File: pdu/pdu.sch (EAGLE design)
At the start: 14 parts, among them IC1 FDN359BN, IC2 FDN359BN, IC3 FDN359BN

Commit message: add usb c (optional)
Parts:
- added C14: 100n, Capacitor:C_CHIP-0603(1608-METRIC)
- added C15: 1u, Capacitor:C_CHIP-0603(1608-METRIC)
- added D2: USBDiode, adafruit:DIODE_SOD-123FL
- added J6: USB4105-GF-A, USB4105-GF-A:USB4105-GF-A
- added R12, R14: 5k1, Resistor:R_CHIP-0603(1608-METRIC)
- added R13: 1M, Resistor:R_CHIP-0603(1608-METRIC)
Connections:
- net N$4 renamed RET
- new net CC1: J6.CC1, R14.1
- new net CC2: J6.CC2, R12.1
- new net SHLD: J6.SHELL_GND, R13.1
- new net VBUS: C14.2, C15.2, D2.A, J6.VBUS
- net GND: now also C14.1, C15.1, J6.GND, R12.2, R13.2, R14.2
- net VBAT: now also D2.C
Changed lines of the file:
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@@
 <part name="SUPPLY6" library="Power_Symbols" library_urn="urn:adsk.eagle:library:16502351" deviceset="GND-BAR" device="" value="GND"/>
 <part name="C3" library="Capacitor" library_urn="urn:adsk.eagle:library:16290819" deviceset="C" device="CHIP-0603(1608-METRIC)" package3d_urn="urn:adsk.eagle:package:16290898/5" technology="_" value="100p"/>
+<part name="SUPPLY24" library="Power_Symbols" library_urn="urn:adsk.eagle:library:16502351" deviceset="GND-BAR" device="" value="GND"/>
+<part name="R12" library="Resistor" library_urn="urn:adsk.eagle:library:16378527" deviceset="R" device="CHIP-0603(1608-METRIC)" package3d_urn="urn:adsk.eagle:package:16378565/5" technology="_" value="5k1"/>
+<part name="R13" library="Resistor" library_urn="urn:adsk.eagle:library:16378527" deviceset="R" device="CHIP-0603(1608-METRIC)" package3d_urn="urn:adsk.eagle:package:16378565/5" technology="_" value="1M"/>
+<part name="R14" library="Resistor" library_urn="urn:adsk.eagle:library:16378527" deviceset="R" device="CHIP-0603(1608-METRIC)" package3d_urn="urn:adsk.eagle:package:16378565/5" technology="_" value="5k1"/>
+<part name="D2" library="adafruit" library_urn="urn:adsk.eagle:library:420" deviceset="DIODE" device="_SOD-123FL" package3d_urn="urn:adsk.eagle:package:6240937/1" override_package3d_urn="urn:adsk.eagle:package:44099330/2" override_package_urn="urn:adsk.eagle:footprint:6240294/1" value="USBDiode"/>
+<part name="C14" library="Capacitor" library_urn="urn:adsk.eagle:library:16290819" deviceset="C" device="CHIP-0603(1608-METRIC)" package3d_urn="urn:adsk.eagle:package:16290898/5" technology="_" value="100n"/>
+<part name="C15" library="Capacitor" library_urn="urn:adsk.eagle:library:16290819" deviceset="C" device="CHIP-0603(1608-METRIC)" package3d_urn="urn:adsk.eagle:package:16290898/5" technology="_" value="1u"/>
+<part name="J6" library="USB4105-GF-A" deviceset="USB4105-GF-A" device=""/>
+<part name="SUPPLY48" library="Power_Symbols" library_urn="urn:adsk.eagle:library:16502351" deviceset="GND-BAR" device="" value="GND"/>
 </parts>
 <sheets>
@@
 <attribute name="NAME" x="-6.985" y="-71.755" size="1.778" layer="95" rot="R180"/>
 <attribute name="VALUE" x="-8.255" y="-67.31" size="1.778" layer="96" rot="R180"/>
+</instance>
+<instance part="SUPPLY24" gate="G$1" x="6.35" y="100.33" smashed="yes">
+<attribute name="VALUE" x="6.35" y="98.425" size="1.778" layer="96" align="center"/>
+</instance>
+<instance part="R12" gate="G$1" x="24.13" y="113.03" smashed="yes" rot="R270">
+<attribute name="NAME" x="26.67" y="113.03" size="1.778" layer="95" rot="R270" align="center"/>
+<attribute name="VALUE" x="21.59" y="113.03" size="1.778" layer="96" rot="R270" align="center"/>
+</instance>
+<instance part="R13" gate="G$1" x="13.97" y="113.03" smashed="yes" rot="R270">
+<attribute name="NAME" x="16.51" y="113.03" size="1.778" layer="95" rot="R270" align="center"/>
+<attribute name="VALUE" x="11.43" y="113.03" size="1.778" layer="96" rot="R270" align="center"/>
+</instance>
+<instance part="R14" gate="G$1" x="34.29" y="113.03" smashed="yes" rot="R270">
+<attribute name="NAME" x="36.83" y="113.03" size="1.778" layer="95" rot="R270" align="center"/>
+<attribute name="VALUE" x="31.75" y="113.03" size="1.778" layer="96" rot="R270" align="center"/>
+</instance>
+<instance part="D2" gate="G$1" x="19.05" y="138.43" smashed="yes">
+<attribute name="NAME" x="16.51" y="140.97" size="1.27" layer="95"/>
+<attribute name="VALUE" x="16.51" y="134.62" size="1.27" layer="96"/>
+</instance>
+<instance part="C14" gate="G$1" x="54.61" y="110.49" smashed="yes" rot="R180">
+<attribute name="NAME" x="60.325" y="109.855" size="1.778" layer="95" rot="R180"/>
+<attribute name="VALUE" x="60.325" y="116.84" size="1.778" layer="96" rot="R180"/>
+</instance>
+<instance part="C15" gate="G$1" x="44.45" y="110.49" smashed="yes" rot="R180">
+<attribute name="NAME" x="50.165" y="109.855" size="1.778" layer="95" rot="R180"/>
+<attribute name="VALUE" x="47.625" y="116.84" size="1.778" layer="96" rot="R180"/>
+</instance>
+<instance part="J6" gate="G$1" x="-49.53" y="124.46" smashed="yes">
+<attribute name="NAME" x="-64.77" y="138.43" size="1.778" layer="95"/>
+<attribute name="VALUE" x="-64.77" y="109.22" size="1.778" layer="96"/>
+</instance>
+<instance part="SUPPLY48" gate="G$1" x="-8.89" y="116.84" smashed="yes" rot="R90">
+<attribute name="VALUE" x="-6.985" y="116.84" size="1.778" layer="96" rot="R90" align="center"/>
 </instance>
 </instances>
@@
 <junction x="0" y="-77.47"/>
 </segment>
+<segment>
+<wire x1="1.27" y1="123.19" x2="6.35" y2="123.19" width="0.1524" layer="91"/>
+<pinref part="SUPPLY24" gate="G$1" pin="GND"/>
+<wire x1="6.35" y1="123.19" x2="6.35" y2="105.41" width="0.1524" layer="91"/>
+<pinref part="R13" gate="G$1" pin="2"/>
+<wire x1="6.35" y1="105.41" x2="6.35" y2="102.87" width="0.1524" layer="91"/>
+<wire x1="13.97" y1="107.95" x2="13.97" y2="105.41" width="0.1524" layer="91"/>
+<wire x1="13.97" y1="105.41" x2="6.35" y2="105.41" width="0.1524" layer="91"/>
+<junction x="6.35" y="105.41"/>
+<pinref part="R14" gate="G$1" pin="2"/>
+<wire x1="34.29" y1="107.95" x2="34.29" y2="105.41" width="0.1524" layer="91"/>
+<wire x1="34.29" y1="105.41" x2="24.13" y2="105.41" width="0.1524" layer="91"/>
+<junction x="13.97" y="105.41"/>
+<pinref part="R12" gate="G$1" pin="2"/>
+<wire x1="24.13" y1="105.41" x2="13.97" y2="105.41" width="0.1524" layer="91"/>
+<wire x1="24.13" y1="107.95" x2="24.13" y2="105.41" width="0.1524" layer="91"/>
+<junction x="24.13" y="105.41"/>
+<pinref part="C15" gate="G$1" pin="1"/>
+<wire x1="44.45" y1="107.95" x2="44.45" y2="105.41" width="0.1524" layer="91"/>
+<wire x1="44.45" y1="105.41" x2="34.29" y2="105.41" width="0.1524" layer="91"/>
+<junction x="34.29" y="105.41"/>
+<pinref part="C14" gate="G$1" pin="1"/>
+<wire x1="54.61" y1="107.95" x2="54.61" y2="105.41" width="0.1524" layer="91"/>
+<wire x1="54.61" y1="105.41" x2="44.45" y2="105.41" width="0.1524" layer="91"/>
+<junction x="44.45" y="105.41"/>
+</segment>
+<segment>
+<pinref part="J6" gate="G$1" pin="GND"/>
+<wire x1="-29.21" y1="116.84" x2="-11.43" y2="116.84" width="0.1524" layer="91"/>
+<pinref part="SUPPLY48" gate="G$1" pin="GND"/>
+</segment>
 </net>
 <net name="VBAT" class="0">
@@
 <label x="35.56" y="72.39" size="1.778" layer="95"/>
 </segment>
+<segment>
+<pinref part="D2" gate="G$1" pin="C"/>
+<wire x1="21.59" y1="138.43" x2="38.1" y2="138.43" width="0.1524" layer="91"/>
+<label x="31.75" y="139.7" size="1.778" layer="95"/>
+</segment>
 </net>
 <net name="EN" class="0">
@@
 </segment>
 </net>
-<net name="N$4" class="0">
+<net name="RET" class="0">
 <segment>
 <pinref part="IC3" gate="G$1" pin="D"/>
@@
 <junction x="20.32" y="-30.48"/>
 <wire x1="20.32" y1="-30.48" x2="57.15" y2="-30.48" width="0.1524" layer="91"/>
+<label x="50.8" y="-30.48" size="1.778" layer="95"/>
+</segment>
+</net>
+<net name="SHLD" class="0">
+<segment>
+<pinref part="R13" gate="G$1" pin="1"/>
+<wire x1="1.27" y1="125.73" x2="13.97" y2="125.73" width="0.1524" layer="91"/>
+<wire x1="13.97" y1="125.73" x2="13.97" y2="118.11" width="0.1524" layer="91"/>
+<label x="3.81" y="125.73" size="1.778" layer="95"/>
+</segment>
+<segment>
+<pinref part="J6" gate="G$1" pin="SHELL_GND"/>
+<wire x1="-29.21" y1="114.3" x2="-19.05" y2="114.3" width="0.1524" layer="91"/>
+<label x="-26.67" y="111.76" size="1.778" layer="95"/>
+</segment>
+</net>
+<net name="CC2" class="0">
+<segment>
+<wire x1="1.27" y1="128.27" x2="24.13" y2="128.27" width="0.1524" layer="91"/>
+<pinref part="R12" gate="G$1" pin="1"/>
+<wire x1="24.13" y1="128.27" x2="24.13" y2="118.11" width="0.1524" layer="91"/>
+<label x="3.81" y="128.27" size="1.778" layer="95"/>
+</segment>
+<segment>
+<pinref part="J6" gate="G$1" pin="CC2"/>
+<wire x1="-29.21" y1="129.54" x2="-19.05" y2="129.54" width="0.1524" layer="91"/>
+<label x="-19.05" y="129.54" size="1.778" layer="95"/>
+</segment>
+</net>
+<net name="CC1" class="0">
+<segment>
+<pinref part="R14" gate="G$1" pin="1"/>
+<wire x1="1.27" y1="130.81" x2="34.29" y2="130.81" width="0.1524" layer="91"/>
+<wire x1="34.29" y1="130.81" x2="34.29" y2="118.11" width="0.1524" layer="91"/>
+<label x="3.81" y="130.81" size="1.778" layer="95"/>
+</segment>
+<segment>
+<pinref part="J6" gate="G$1" pin="CC1"/>
+<wire x1="-69.85" y1="129.54" x2="-82.55" y2="129.54" width="0.1524" layer="91"/>
+<label x="-82.55" y="129.54" size="1.778" layer="95"/>
+</segment>
+</net>
+<net name="VBUS" class="0">
+<segment>
+<pinref part="D2" gate="G$1" pin="A"/>
+<wire x1="1.27" y1="138.43" x2="11.43" y2="138.43" width="0.1524" layer="91"/>
+<wire x1="11.43" y1="138.43" x2="16.51" y2="138.43" width="0.1524" layer="91"/>
+<junction x="11.43" y="138.43"/>
+<wire x1="11.43" y1="138.43" x2="11.43" y2="133.35" width="0.1524" layer="91"/>
+<wire x1="11.43" y1="133.35" x2="44.45" y2="133.35" width="0.1524" layer="91"/>
+<pinref part="C14" gate="G$1" pin="2"/>
+<wire x1="44.45" y1="133.35" x2="54.61" y2="133.35" width="0.1524" layer="91"/>
+<wire x1="54.61" y1="133.35" x2="54.61" y2="115.57" width="0.1524" layer="91"/>
+<pinref part="C15" gate="G$1" pin="2"/>
+<wire x1="44.45" y1="115.57" x2="44.45" y2="133.35" width="0.1524" layer="91"/>
+<junction x="44.45" y="133.35"/>
+<label x="1.27" y="138.43" size="1.778" layer="95"/>
+</segment>
+<segment>
+<pinref part="J6" gate="G$1" pin="VBUS"/>
+<wire x1="-29.21" y1="134.62" x2="-19.05" y2="134.62" width="0.1524" layer="91"/>
+<label x="-19.05" y="134.62" size="1.778" layer="95"/>
 </segment>
 </net>
@@
 packages will not be understood (or retained) with this version.
 </note>
+<note version="9.4" severity="warning">
+Since Version 9.4, EAGLE supports the overriding of 3D packages
+in schematics and board files. Those overridden 3d packages
+will not be understood (or retained) with this version.
+</note>
 </compatibility>

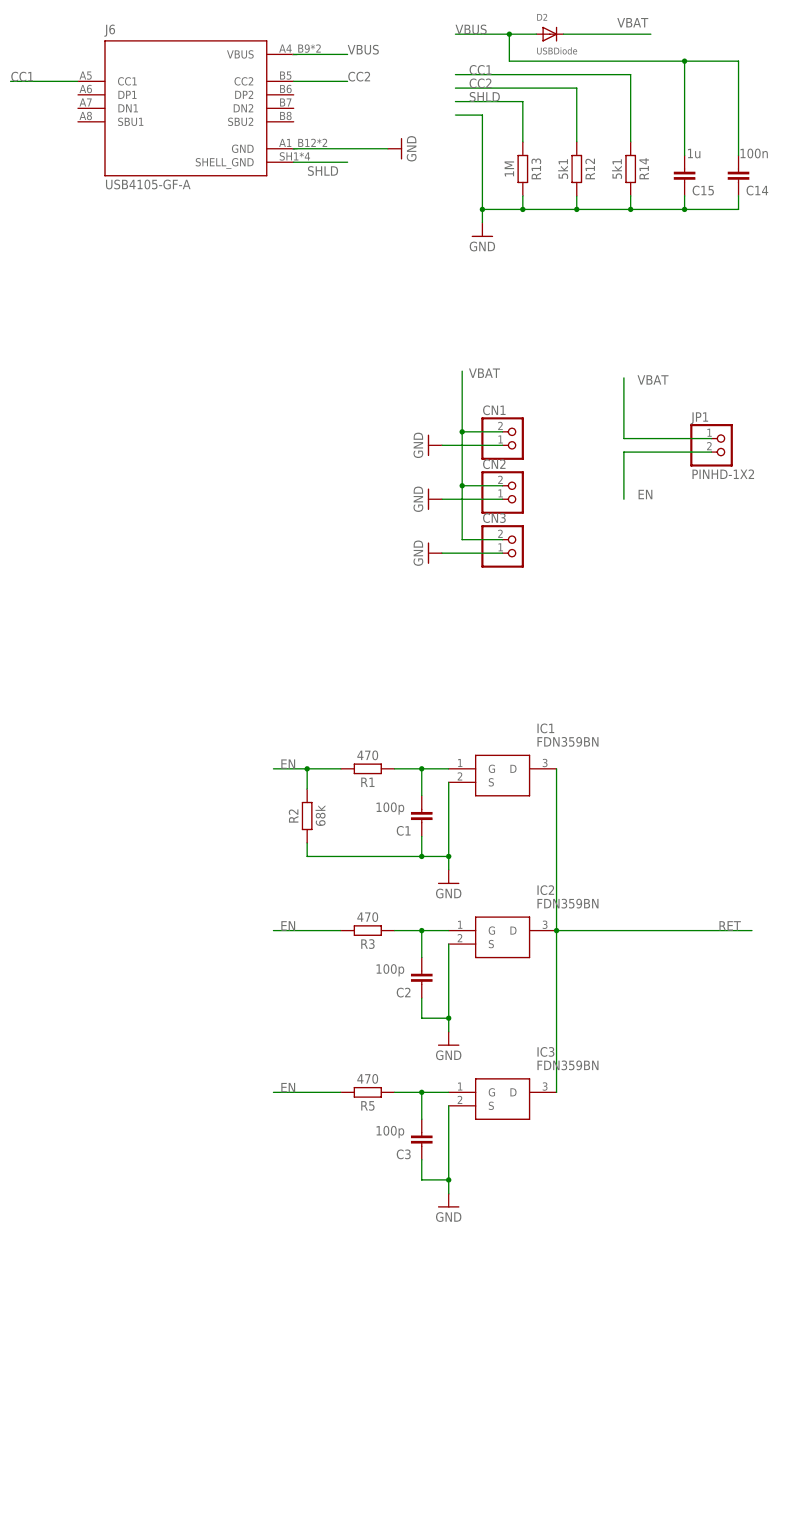
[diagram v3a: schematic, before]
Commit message: add output with decoupling cap
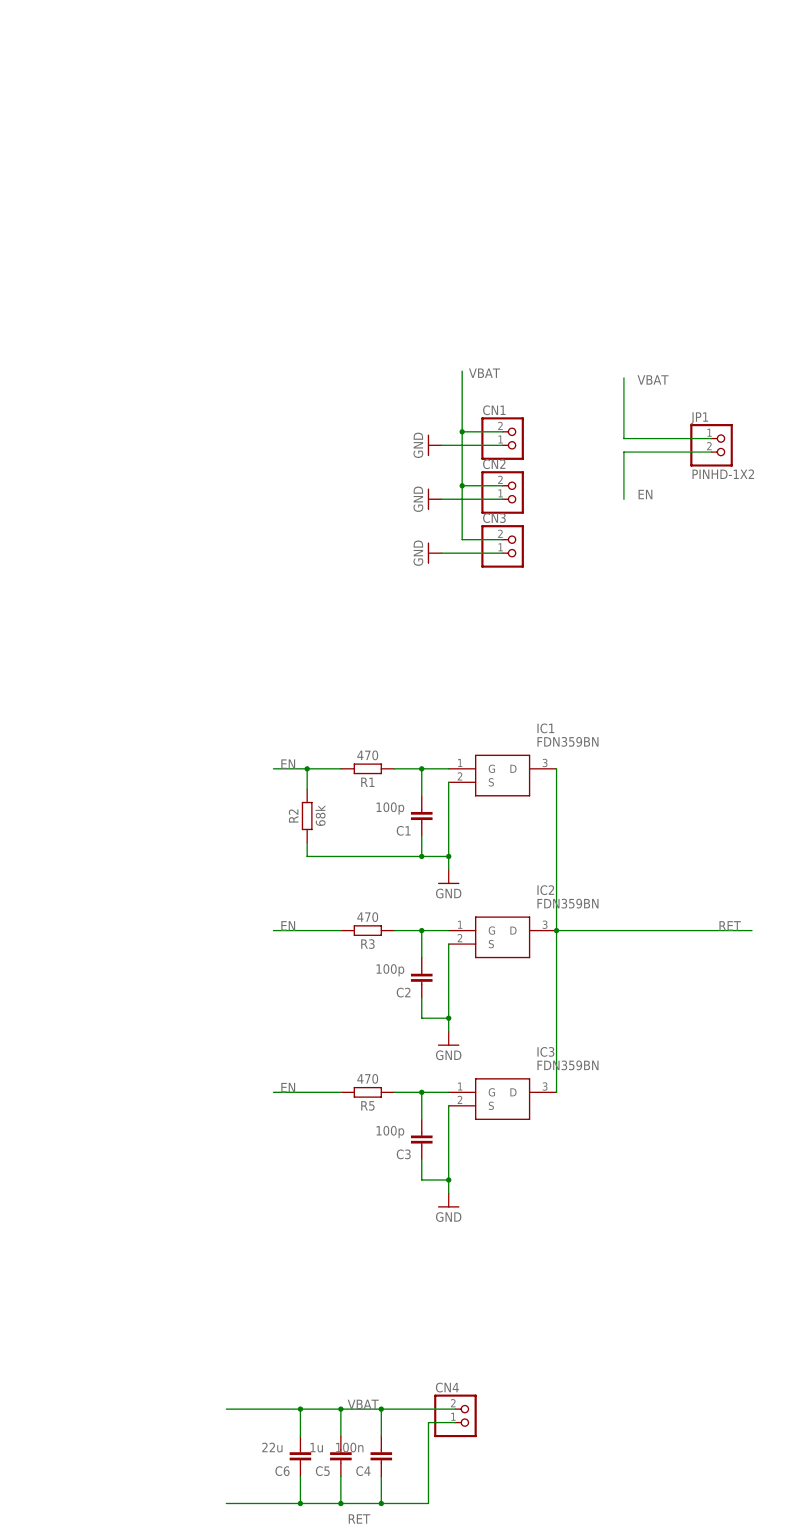
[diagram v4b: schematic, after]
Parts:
- removed C14: 100n, Capacitor:C_CHIP-0603(1608-METRIC)
- removed C15: 1u, Capacitor:C_CHIP-0603(1608-METRIC)
- removed D2: USBDiode, adafruit:DIODE_SOD-123FL
- removed J6: USB4105-GF-A, USB4105-GF-A:USB4105-GF-A
- removed R12, R14: 5k1, Resistor:R_CHIP-0603(1608-METRIC)
- removed R13: 1M, Resistor:R_CHIP-0603(1608-METRIC)
- added C4: 100n, Capacitor:C_CHIP-0603(1608-METRIC)
- added C5: 1u, Capacitor:C_CHIP-0603(1608-METRIC)
- added C6: 22u, Capacitor:C_CHIP-0603(1608-METRIC)
- added CN4: (no value), adafruit:JST_2PIN-THM-RA
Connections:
- removed net CC1: J6.CC1, R14.1
- removed net CC2: J6.CC2, R12.1
- removed net SHLD: J6.SHELL_GND, R13.1
- removed net VBUS: C14.2, C15.2, D2.A, J6.VBUS
- net GND: no longer C14.1, C15.1, J6.GND, R12.2, R13.2, R14.2
- net RET: now also C4.1, C5.1, C6.1, CN4.2
- net VBAT: now also C4.2, C5.2, C6.2, CN4.1; no longer D2.C
